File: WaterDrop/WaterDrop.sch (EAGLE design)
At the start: 12 parts, among them IC1 PIC12F1822

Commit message: random cotroller added
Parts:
- added D1: SD0, WaterDrop:SD0
- added X1, X2: P-PAD-S, OSSI:P-PAD-S
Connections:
- net +5V: now also D1.P$1
- net GND: now also D1.P$2, X2.P$1
- net PIEZO: now also X1.P$1
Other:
- note removed: "Reverse Voltage Protection"
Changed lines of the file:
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@@
 <part name="JP2" library="SparkFun-Connectors" deviceset="M02" device="PTH"/>
 <part name="JP3" library="WaterDrop" deviceset="2PIN" device=""/>
+<part name="X1" library="OSSI" deviceset="P-PAD" device="-S"/>
+<part name="X2" library="OSSI" deviceset="P-PAD" device="-S"/>
+<part name="D1" library="WaterDrop" deviceset="SD0" device=""/>
 </parts>
 <sheets>
@@
 <plain>
 <text x="25.4" y="99.06" size="1.778" layer="91">ESD Guard</text>
-<text x="86.36" y="116.84" size="1.778" layer="91">Reverse Voltage Protection</text>
 </plain>
 <instances>
@@
 <instance part="JP2" gate="G$1" x="93.98" y="137.16" rot="R270"/>
 <instance part="JP3" gate="G$1" x="157.48" y="83.82" rot="R180"/>
+<instance part="X1" gate="G$1" x="147.32" y="99.06" rot="R90"/>
+<instance part="X2" gate="G$1" x="147.32" y="63.5" rot="R270"/>
+<instance part="D1" gate="G$1" x="96.52" y="116.84"/>
 </instances>
 <busses>
@@
 <pinref part="C2" gate="G$1" pin="1"/>
 <wire x1="88.9" y1="106.68" x2="93.98" y2="106.68" width="0.1524" layer="91"/>
-<wire x1="88.9" y1="106.68" x2="88.9" y2="121.92" width="0.1524" layer="91"/>
+<wire x1="88.9" y1="106.68" x2="88.9" y2="116.84" width="0.1524" layer="91"/>
 <junction x="88.9" y="106.68"/>
 <pinref part="JP2" gate="G$1" pin="1"/>
+<wire x1="88.9" y1="116.84" x2="88.9" y2="121.92" width="0.1524" layer="91"/>
 <wire x1="88.9" y1="121.92" x2="93.98" y2="121.92" width="0.1524" layer="91"/>
 <wire x1="93.98" y1="121.92" x2="93.98" y2="129.54" width="0.1524" layer="91"/>
+<pinref part="D1" gate="G$1" pin="P$1"/>
+<wire x1="91.44" y1="116.84" x2="88.9" y2="116.84" width="0.1524" layer="91"/>
+<junction x="88.9" y="116.84"/>
 </segment>
 <segment>
@@
 <wire x1="96.52" y1="129.54" x2="96.52" y2="121.92" width="0.1524" layer="91"/>
 <wire x1="96.52" y1="121.92" x2="109.22" y2="121.92" width="0.1524" layer="91"/>
-<wire x1="109.22" y1="121.92" x2="109.22" y2="106.68" width="0.1524" layer="91"/>
+<wire x1="109.22" y1="121.92" x2="109.22" y2="116.84" width="0.1524" layer="91"/>
 <junction x="109.22" y="106.68"/>
+<pinref part="D1" gate="G$1" pin="P$2"/>
+<wire x1="109.22" y1="116.84" x2="109.22" y2="106.68" width="0.1524" layer="91"/>
+<wire x1="106.68" y1="116.84" x2="109.22" y2="116.84" width="0.1524" layer="91"/>
+<junction x="109.22" y="116.84"/>
 </segment>
 <segment>
@@
 <wire x1="119.38" y1="78.74" x2="137.16" y2="78.74" width="0.1524" layer="91"/>
 <wire x1="137.16" y1="78.74" x2="137.16" y2="81.28" width="0.1524" layer="91"/>
-<wire x1="137.16" y1="81.28" x2="149.86" y2="81.28" width="0.1524" layer="91"/>
+<wire x1="137.16" y1="81.28" x2="147.32" y2="81.28" width="0.1524" layer="91"/>
 <pinref part="JP3" gate="G$1" pin="2"/>
+<pinref part="X2" gate="G$1" pin="P$1"/>
+<wire x1="147.32" y1="81.28" x2="149.86" y2="81.28" width="0.1524" layer="91"/>
+<wire x1="147.32" y1="68.58" x2="147.32" y2="81.28" width="0.1524" layer="91"/>
+<junction x="147.32" y="81.28"/>
 </segment>
 <segment>
@@
 <wire x1="106.68" y1="83.82" x2="119.38" y2="83.82" width="0.1524" layer="91"/>
 <label x="119.38" y="83.82" size="1.778" layer="95" xref="yes"/>
-<wire x1="119.38" y1="83.82" x2="149.86" y2="83.82" width="0.1524" layer="91"/>
+<wire x1="119.38" y1="83.82" x2="147.32" y2="83.82" width="0.1524" layer="91"/>
 <pinref part="JP3" gate="G$1" pin="1"/>
+<pinref part="X1" gate="G$1" pin="P$1"/>
+<wire x1="147.32" y1="83.82" x2="149.86" y2="83.82" width="0.1524" layer="91"/>
+<wire x1="147.32" y1="93.98" x2="147.32" y2="83.82" width="0.1524" layer="91"/>
+<junction x="147.32" y="83.82"/>
 </segment>
 </net>

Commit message: waterdrop and random controller gerber
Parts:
- removed X1, X2: P-PAD-S, OSSI:P-PAD-S
- added U$1: LOGOPIEZO, WaterDrop:LOGOPIEZO
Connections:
- net GND: no longer X2.P$1
- net PIEZO: no longer X1.P$1
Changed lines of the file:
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@@
 <part name="JP2" library="SparkFun-Connectors" deviceset="M02" device="PTH"/>
 <part name="JP3" library="WaterDrop" deviceset="2PIN" device=""/>
-<part name="X1" library="OSSI" deviceset="P-PAD" device="-S"/>
-<part name="X2" library="OSSI" deviceset="P-PAD" device="-S"/>
 <part name="D1" library="WaterDrop" deviceset="SD0" device=""/>
+<part name="U$1" library="WaterDrop" deviceset="LOGO" device="PIEZO"/>
 </parts>
 <sheets>
@@
 <instance part="JP2" gate="G$1" x="93.98" y="137.16" rot="R270"/>
 <instance part="JP3" gate="G$1" x="157.48" y="83.82" rot="R180"/>
-<instance part="X1" gate="G$1" x="147.32" y="99.06" rot="R90"/>
-<instance part="X2" gate="G$1" x="147.32" y="63.5" rot="R270"/>
 <instance part="D1" gate="G$1" x="96.52" y="116.84"/>
+<instance part="U$1" gate="G$1" x="144.78" y="111.76"/>
 </instances>
 <busses>
@@
 <wire x1="137.16" y1="81.28" x2="147.32" y2="81.28" width="0.1524" layer="91"/>
 <pinref part="JP3" gate="G$1" pin="2"/>
-<pinref part="X2" gate="G$1" pin="P$1"/>
 <wire x1="147.32" y1="81.28" x2="149.86" y2="81.28" width="0.1524" layer="91"/>
-<wire x1="147.32" y1="68.58" x2="147.32" y2="81.28" width="0.1524" layer="91"/>
-<junction x="147.32" y="81.28"/>
 </segment>
 <segment>
@@
 <wire x1="119.38" y1="83.82" x2="147.32" y2="83.82" width="0.1524" layer="91"/>
 <pinref part="JP3" gate="G$1" pin="1"/>
-<pinref part="X1" gate="G$1" pin="P$1"/>
 <wire x1="147.32" y1="83.82" x2="149.86" y2="83.82" width="0.1524" layer="91"/>
-<wire x1="147.32" y1="93.98" x2="147.32" y2="83.82" width="0.1524" layer="91"/>
-<junction x="147.32" y="83.82"/>
 </segment>
 </net>

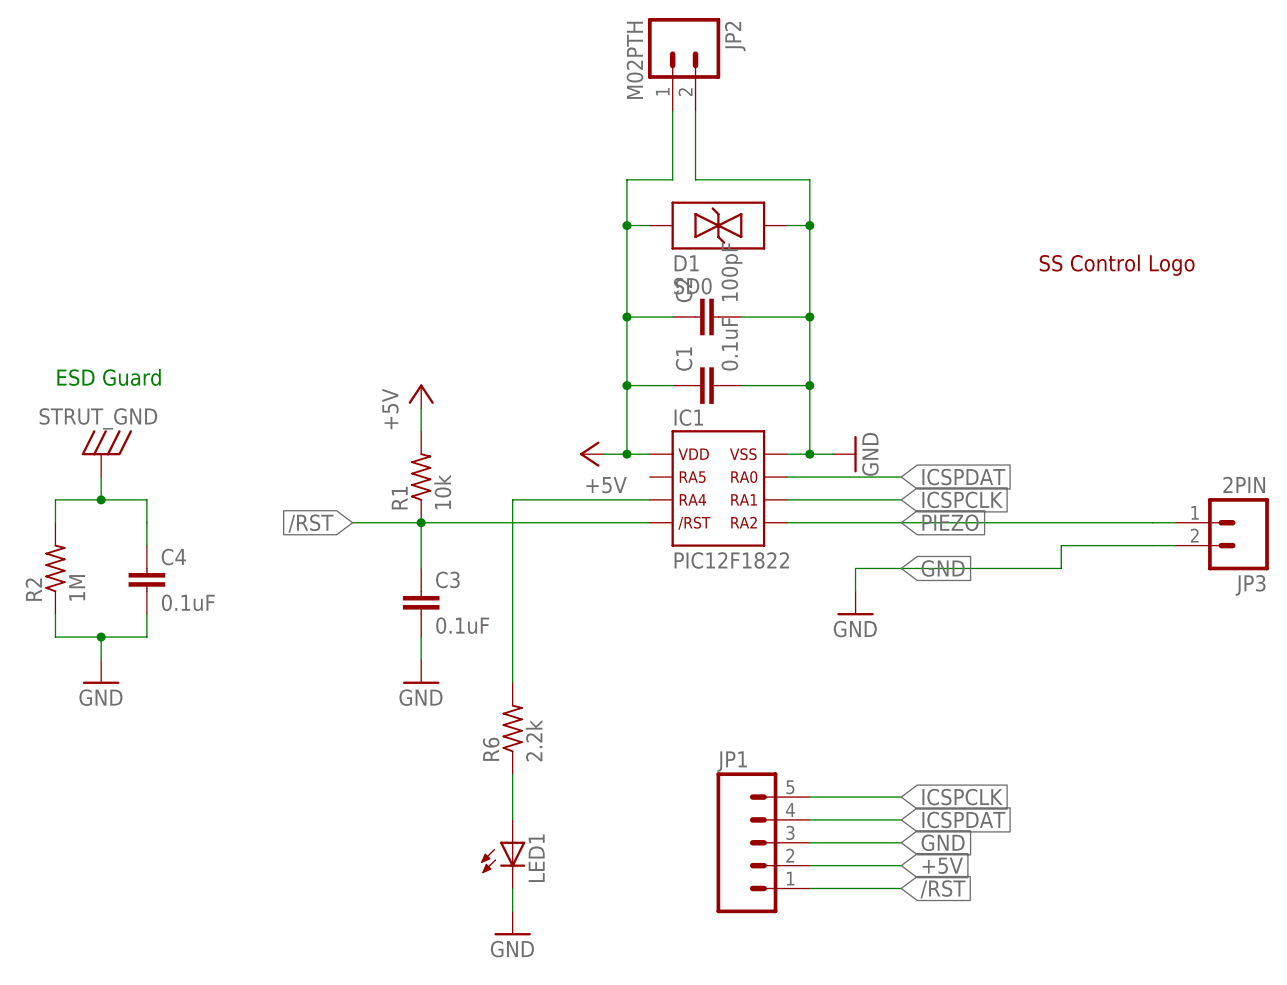
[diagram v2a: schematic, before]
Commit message: schmatic renumbered final merged gerber for fab
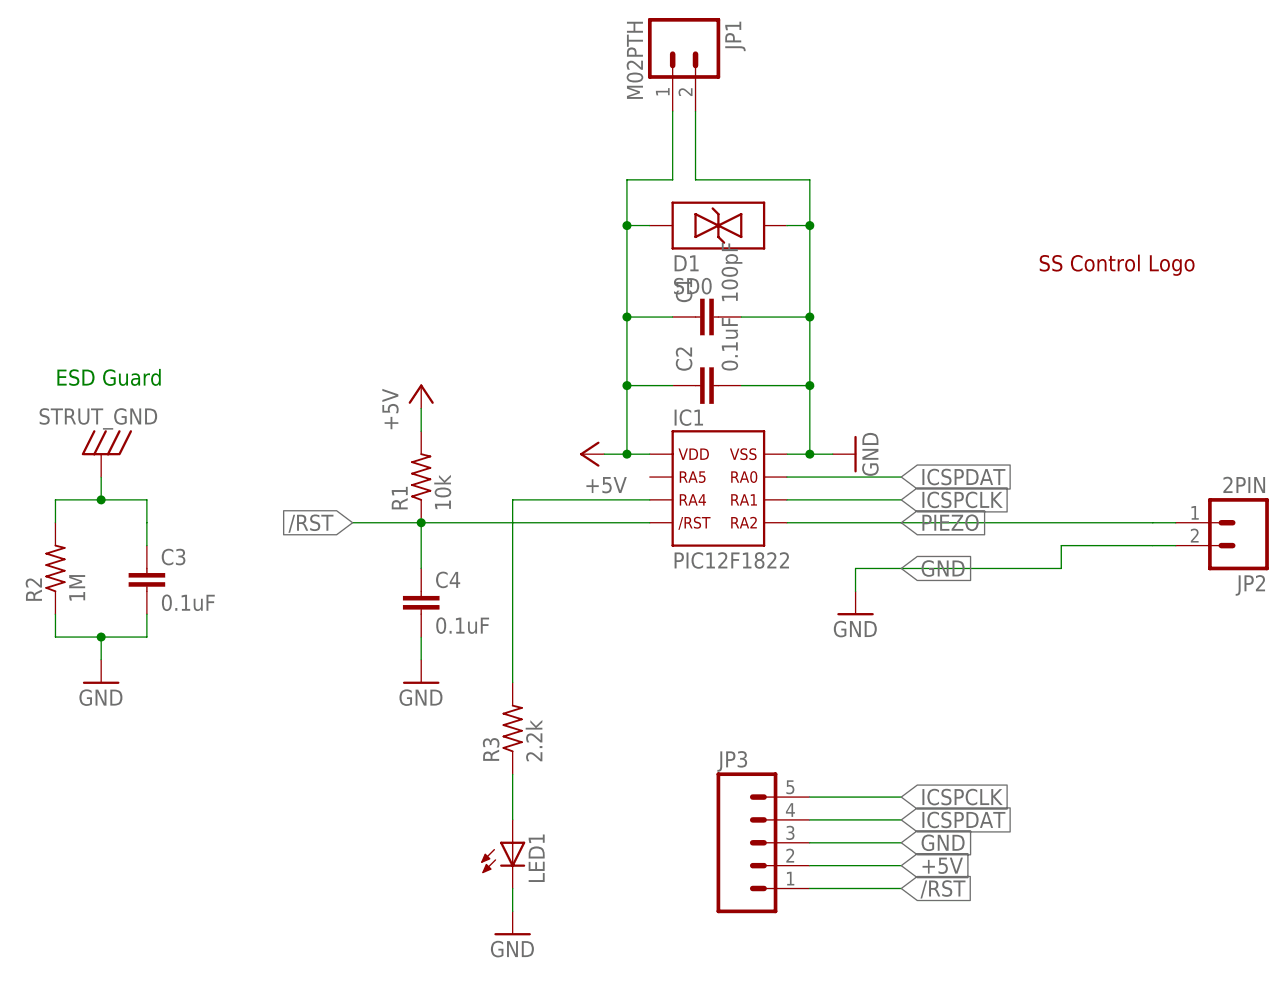
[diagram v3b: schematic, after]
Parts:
- C1: value 0.1uF -> 100pF
- C2: value 100pF -> 0.1uF
- JP1: value (none) -> M02PTH; device SparkFun-Connectors:M05PTH -> SparkFun-Connectors:M02PTH
- JP2: value M02PTH -> 2PIN; device SparkFun-Connectors:M02PTH -> WaterDrop:2PIN
- JP3: value 2PIN -> (none); device WaterDrop:2PIN -> SparkFun-Connectors:M05PTH
- renumbered R6 to R3
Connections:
- net +5V: now also JP1.1, JP3.2; no longer JP1.2, JP2.1
- net /RST: now also C4.1, JP3.1; no longer C3.1, JP1.1
- net GND: now also JP1.2, JP3.3; no longer JP1.3, JP3.2
- net ICSPCLK: now also JP3.5; no longer JP1.5
- net ICSPDAT: now also JP3.4; no longer JP1.4
- net PIEZO: now also JP2.1; no longer JP3.1
- net STRUT_GND: now also C3.1; no longer C4.1
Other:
- moved on the sheet: C1, C2, C3, C4, JP2
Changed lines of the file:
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@@
 <part name="P+1" library="supply1" deviceset="+5V" device=""/>
 <part name="GND1" library="supply1" deviceset="GND" device=""/>
-<part name="C1" library="WaterDrop" deviceset="C" device="0603(1608)" value="0.1uF"/>
-<part name="C2" library="WaterDrop" deviceset="C" device="0603(1608)" value="100pF"/>
+<part name="C2" library="WaterDrop" deviceset="C" device="0603(1608)" value="0.1uF"/>
+<part name="C1" library="WaterDrop" deviceset="C" device="0603(1608)" value="100pF"/>
 <part name="GND2" library="supply1" deviceset="GND" device=""/>
 <part name="R1" library="WaterDrop" deviceset="R" device="0603(1608)" value="10k"/>
-<part name="C3" library="WaterDrop" deviceset="C" device="0603(1608)" value="0.1uF"/>
+<part name="C4" library="WaterDrop" deviceset="C" device="0603(1608)" value="0.1uF"/>
 <part name="P+2" library="supply1" deviceset="+5V" device=""/>
 <part name="GND3" library="supply1" deviceset="GND" device=""/>
@@
 <part name="GND4" library="supply1" deviceset="GND" device=""/>
 <part name="R2" library="WaterDrop" deviceset="R" device="0603(1608)" value="1M"/>
-<part name="C4" library="WaterDrop" deviceset="C" device="0603(1608)" value="0.1uF"/>
+<part name="C3" library="WaterDrop" deviceset="C" device="0603(1608)" value="0.1uF"/>
 <part name="LED1" library="SparkFun" deviceset="LED" device="0603"/>
-<part name="R6" library="WaterDrop" deviceset="R" device="0603(1608)" value="2.2k"/>
+<part name="R3" library="WaterDrop" deviceset="R" device="0603(1608)" value="2.2k"/>
 <part name="GND7" library="supply1" deviceset="GND" device=""/>
-<part name="JP1" library="SparkFun-Connectors" deviceset="M05" device="PTH"/>
-<part name="JP2" library="SparkFun-Connectors" deviceset="M02" device="PTH"/>
-<part name="JP3" library="WaterDrop" deviceset="2PIN" device=""/>
+<part name="JP3" library="SparkFun-Connectors" deviceset="M05" device="PTH"/>
+<part name="JP1" library="SparkFun-Connectors" deviceset="M02" device="PTH"/>
+<part name="JP2" library="WaterDrop" deviceset="2PIN" device=""/>
 <part name="D1" library="WaterDrop" deviceset="SD0" device=""/>
 <part name="U$1" library="WaterDrop" deviceset="LOGO" device="PIEZO"/>
@@
 <instance part="P+1" gate="1" x="83.82" y="91.44" rot="R90"/>
 <instance part="GND1" gate="1" x="114.3" y="91.44" rot="R90"/>
-<instance part="C1" gate="G$1" x="96.52" y="99.06" rot="R90"/>
-<instance part="C2" gate="G$1" x="96.52" y="106.68" rot="R90"/>
+<instance part="C2" gate="G$1" x="96.52" y="99.06" rot="R90"/>
+<instance part="C1" gate="G$1" x="96.52" y="106.68" rot="R90"/>
 <instance part="GND2" gate="1" x="114.3" y="73.66"/>
 <instance part="R1" gate="G$1" x="66.04" y="88.9" rot="R90"/>
-<instance part="C3" gate="G$1" x="66.04" y="76.2"/>
+<instance part="C4" gate="G$1" x="66.04" y="76.2"/>
 <instance part="P+2" gate="1" x="66.04" y="99.06"/>
 <instance part="GND3" gate="1" x="66.04" y="66.04"/>
@@
 <instance part="GND4" gate="1" x="30.48" y="66.04"/>
 <instance part="R2" gate="G$1" x="25.4" y="78.74" rot="R90"/>
-<instance part="C4" gate="G$1" x="35.56" y="78.74"/>
+<instance part="C3" gate="G$1" x="35.56" y="78.74"/>
 <instance part="LED1" gate="G$1" x="76.2" y="48.26"/>
-<instance part="R6" gate="G$1" x="76.2" y="60.96" rot="R90"/>
+<instance part="R3" gate="G$1" x="76.2" y="60.96" rot="R90"/>
 <instance part="GND7" gate="1" x="76.2" y="38.1"/>
-<instance part="JP1" gate="G$1" x="101.6" y="48.26"/>
-<instance part="JP2" gate="G$1" x="93.98" y="137.16" rot="R270"/>
-<instance part="JP3" gate="G$1" x="157.48" y="83.82" rot="R180"/>
+<instance part="JP3" gate="G$1" x="101.6" y="48.26"/>
+<instance part="JP1" gate="G$1" x="93.98" y="137.16" rot="R270"/>
+<instance part="JP2" gate="G$1" x="157.48" y="83.82" rot="R180"/>
 <instance part="D1" gate="G$1" x="96.52" y="116.84"/>
 <instance part="U$1" gate="G$1" x="144.78" y="111.76"/>
@@
 <wire x1="91.44" y1="91.44" x2="88.9" y2="91.44" width="0.1524" layer="91"/>
 <wire x1="88.9" y1="91.44" x2="86.36" y2="91.44" width="0.1524" layer="91"/>
-<pinref part="C1" gate="G$1" pin="1"/>
+<pinref part="C2" gate="G$1" pin="1"/>
 <wire x1="93.98" y1="99.06" x2="88.9" y2="99.06" width="0.1524" layer="91"/>
 <wire x1="88.9" y1="99.06" x2="88.9" y2="91.44" width="0.1524" layer="91"/>
@@
 <wire x1="88.9" y1="99.06" x2="88.9" y2="106.68" width="0.1524" layer="91"/>
 <junction x="88.9" y="99.06"/>
-<pinref part="C2" gate="G$1" pin="1"/>
+<pinref part="C1" gate="G$1" pin="1"/>
 <wire x1="88.9" y1="106.68" x2="93.98" y2="106.68" width="0.1524" layer="91"/>
 <wire x1="88.9" y1="106.68" x2="88.9" y2="116.84" width="0.1524" layer="91"/>
 <junction x="88.9" y="106.68"/>
-<pinref part="JP2" gate="G$1" pin="1"/>
+<pinref part="JP1" gate="G$1" pin="1"/>
 <wire x1="88.9" y1="116.84" x2="88.9" y2="121.92" width="0.1524" layer="91"/>
 <wire x1="88.9" y1="121.92" x2="93.98" y2="121.92" width="0.1524" layer="91"/>
@@
 </segment>
 <segment>
-<pinref part="JP1" gate="G$1" pin="2"/>
+<pinref part="JP3" gate="G$1" pin="2"/>
 <wire x1="109.22" y1="45.72" x2="119.38" y2="45.72" width="0.1524" layer="91"/>
 <label x="119.38" y="45.72" size="1.778" layer="95" xref="yes"/>
@@
 <pinref part="GND1" gate="1" pin="GND"/>
 <wire x1="106.68" y1="91.44" x2="109.22" y2="91.44" width="0.1524" layer="91"/>
-<pinref part="C1" gate="G$1" pin="2"/>
+<pinref part="C2" gate="G$1" pin="2"/>
 <wire x1="109.22" y1="91.44" x2="111.76" y2="91.44" width="0.1524" layer="91"/>
 <wire x1="101.6" y1="99.06" x2="109.22" y2="99.06" width="0.1524" layer="91"/>
 <wire x1="109.22" y1="99.06" x2="109.22" y2="91.44" width="0.1524" layer="91"/>
 <junction x="109.22" y="91.44"/>
-<pinref part="C2" gate="G$1" pin="2"/>
+<pinref part="C1" gate="G$1" pin="2"/>
 <wire x1="101.6" y1="106.68" x2="109.22" y2="106.68" width="0.1524" layer="91"/>
 <wire x1="109.22" y1="106.68" x2="109.22" y2="99.06" width="0.1524" layer="91"/>
 <junction x="109.22" y="99.06"/>
-<pinref part="JP2" gate="G$1" pin="2"/>
+<pinref part="JP1" gate="G$1" pin="2"/>
 <wire x1="96.52" y1="129.54" x2="96.52" y2="121.92" width="0.1524" layer="91"/>
 <wire x1="96.52" y1="121.92" x2="109.22" y2="121.92" width="0.1524" layer="91"/>
@@
 <wire x1="137.16" y1="78.74" x2="137.16" y2="81.28" width="0.1524" layer="91"/>
 <wire x1="137.16" y1="81.28" x2="147.32" y2="81.28" width="0.1524" layer="91"/>
-<pinref part="JP3" gate="G$1" pin="2"/>
+<pinref part="JP2" gate="G$1" pin="2"/>
 <wire x1="147.32" y1="81.28" x2="149.86" y2="81.28" width="0.1524" layer="91"/>
 </segment>
 <segment>
 <pinref part="GND3" gate="1" pin="GND"/>
-<pinref part="C3" gate="G$1" pin="2"/>
+<pinref part="C4" gate="G$1" pin="2"/>
 <wire x1="66.04" y1="68.58" x2="66.04" y2="71.12" width="0.1524" layer="91"/>
 </segment>
@@
 <wire x1="30.48" y1="71.12" x2="25.4" y2="71.12" width="0.1524" layer="91"/>
 <wire x1="25.4" y1="71.12" x2="25.4" y2="73.66" width="0.1524" layer="91"/>
-<pinref part="C4" gate="G$1" pin="2"/>
+<pinref part="C3" gate="G$1" pin="2"/>
 <wire x1="30.48" y1="71.12" x2="35.56" y2="71.12" width="0.1524" layer="91"/>
 <wire x1="35.56" y1="71.12" x2="35.56" y2="73.66" width="0.1524" layer="91"/>
@@
 </segment>
 <segment>
-<pinref part="JP1" gate="G$1" pin="3"/>
+<pinref part="JP3" gate="G$1" pin="3"/>
 <wire x1="109.22" y1="48.26" x2="119.38" y2="48.26" width="0.1524" layer="91"/>
 <label x="119.38" y="48.26" size="1.778" layer="95" xref="yes"/>
@@
 <label x="119.38" y="83.82" size="1.778" layer="95" xref="yes"/>
 <wire x1="119.38" y1="83.82" x2="147.32" y2="83.82" width="0.1524" layer="91"/>
-<pinref part="JP3" gate="G$1" pin="1"/>
+<pinref part="JP2" gate="G$1" pin="1"/>
 <wire x1="147.32" y1="83.82" x2="149.86" y2="83.82" width="0.1524" layer="91"/>
 </segment>
@@
 <pinref part="R1" gate="G$1" pin="1"/>
 <wire x1="91.44" y1="83.82" x2="66.04" y2="83.82" width="0.1524" layer="91"/>
-<pinref part="C3" gate="G$1" pin="1"/>
+<pinref part="C4" gate="G$1" pin="1"/>
 <wire x1="66.04" y1="83.82" x2="66.04" y2="78.74" width="0.1524" layer="91"/>
 <junction x="66.04" y="83.82"/>
@@
 </segment>
 <segment>
-<pinref part="JP1" gate="G$1" pin="1"/>
+<pinref part="JP3" gate="G$1" pin="1"/>
 <wire x1="109.22" y1="43.18" x2="119.38" y2="43.18" width="0.1524" layer="91"/>
 <label x="119.38" y="43.18" size="1.778" layer="95" xref="yes"/>
@@
 </segment>
 <segment>
-<pinref part="JP1" gate="G$1" pin="4"/>
+<pinref part="JP3" gate="G$1" pin="4"/>
 <wire x1="109.22" y1="50.8" x2="119.38" y2="50.8" width="0.1524" layer="91"/>
 <label x="119.38" y="50.8" size="1.778" layer="95" xref="yes"/>
@@
 </segment>
 <segment>
-<pinref part="JP1" gate="G$1" pin="5"/>
+<pinref part="JP3" gate="G$1" pin="5"/>
 <wire x1="109.22" y1="53.34" x2="119.38" y2="53.34" width="0.1524" layer="91"/>
 <label x="119.38" y="53.34" size="1.778" layer="95" xref="yes"/>
@@
 <pinref part="IC1" gate="G$1" pin="P$3"/>
 <wire x1="91.44" y1="86.36" x2="76.2" y2="86.36" width="0.1524" layer="91"/>
-<pinref part="R6" gate="G$1" pin="2"/>
+<pinref part="R3" gate="G$1" pin="2"/>
 <wire x1="76.2" y1="66.04" x2="76.2" y2="86.36" width="0.1524" layer="91"/>
 </segment>
@@
 <wire x1="35.56" y1="86.36" x2="35.56" y2="83.82" width="0.1524" layer="91"/>
 <junction x="30.48" y="86.36"/>
-<pinref part="C4" gate="G$1" pin="1"/>
+<pinref part="C3" gate="G$1" pin="1"/>
 <wire x1="35.56" y1="83.82" x2="35.56" y2="81.28" width="0.1524" layer="91"/>
 </segment>
@@
 <segment>
 <pinref part="LED1" gate="G$1" pin="A"/>
-<pinref part="R6" gate="G$1" pin="1"/>
+<pinref part="R3" gate="G$1" pin="1"/>
 <wire x1="76.2" y1="50.8" x2="76.2" y2="55.88" width="0.1524" layer="91"/>
 </segment>
